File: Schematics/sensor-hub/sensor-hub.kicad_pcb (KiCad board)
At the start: 2 copper layers, 66.5 x 135 mm, 85 parts, among them J1 USB_C_Receptacle_USB2.0, J2 Conn_01x03, J3 Conn_01x09_Male, Q1 BC818, Q2 BC818, SW1 SW_Push, SW2 SW_Push, SW3 SW_Push, SW4 SW_Push, SW5 SW_Push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

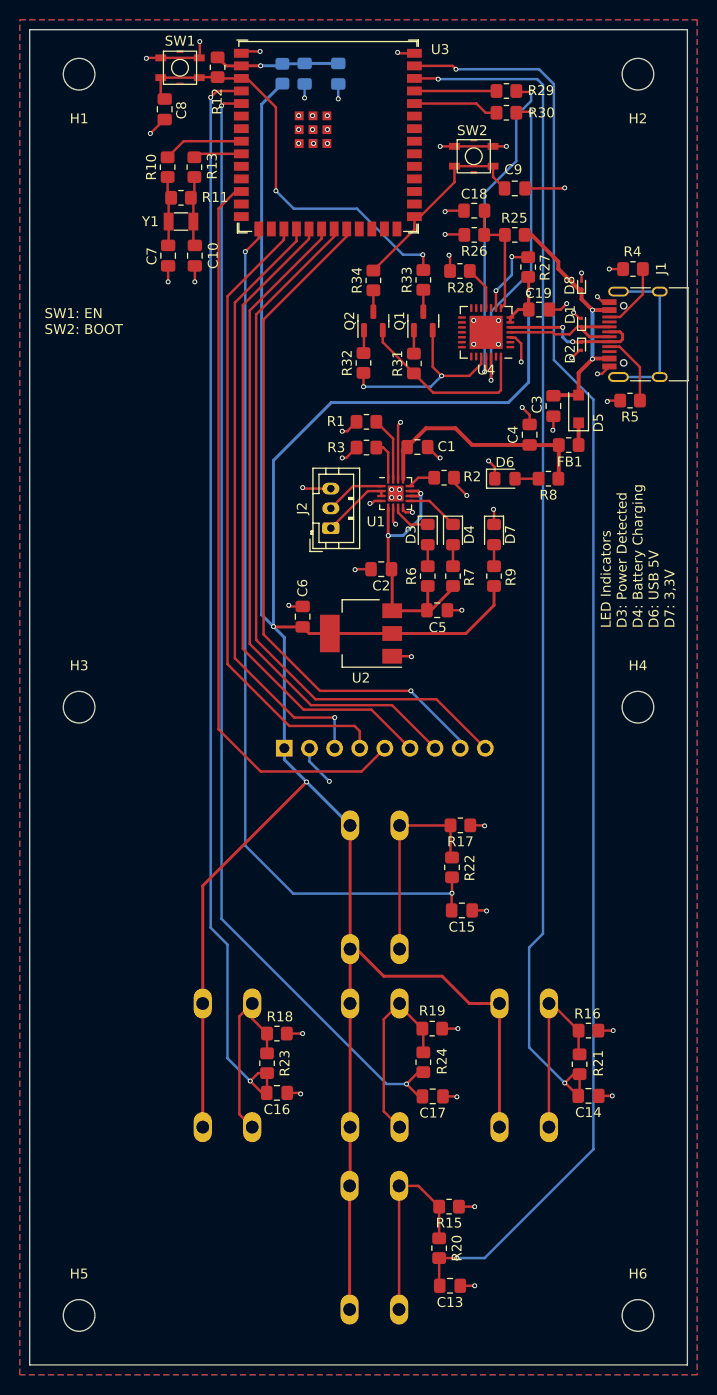
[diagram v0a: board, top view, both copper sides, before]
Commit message: evenly spaced out switches
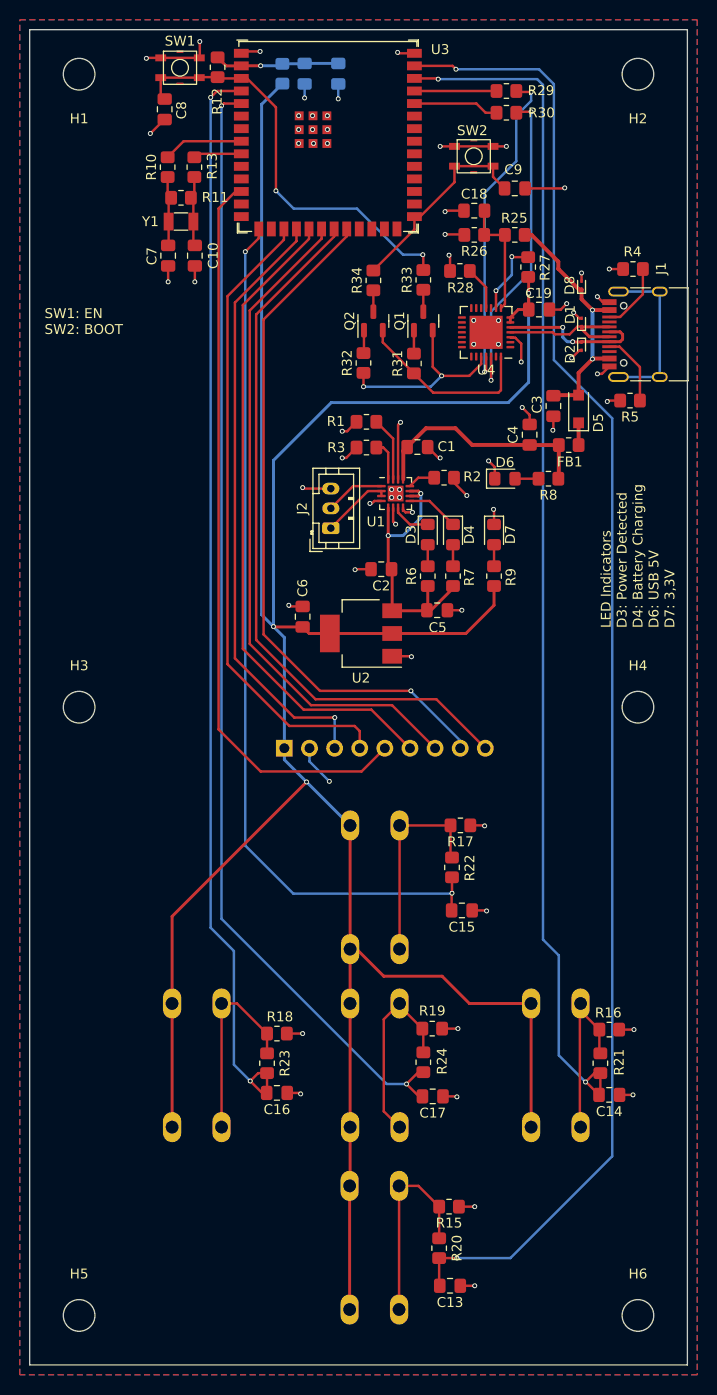
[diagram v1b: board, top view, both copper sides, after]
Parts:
- moved SW4 3.20 mm to (128.2, 124.0)
- moved SW6 3.10 mm to (91.9, 124.0)
- moved C14 2.10 mm to (136.1, 133.2)
- moved R16 2.10 mm to (136.1, 126.6)
- moved R21 2.10 mm to (135.2, 130.0)
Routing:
- net +3V3: track 284.3 -> 288.8 mm
- net SWITCH0: track 147.2 -> 150.3 mm
- net Net-(R18-Pad2): track 19.2 -> 20.4 mm
- net Net-(R16-Pad2): track 19.1 -> 18.4 mm
